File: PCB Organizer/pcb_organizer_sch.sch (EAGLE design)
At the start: 5 parts, among them J1 455-1750-1-ND, U1 ARDUINO_NANO, U2 V8FR-II, U3 POLOLU_TB67

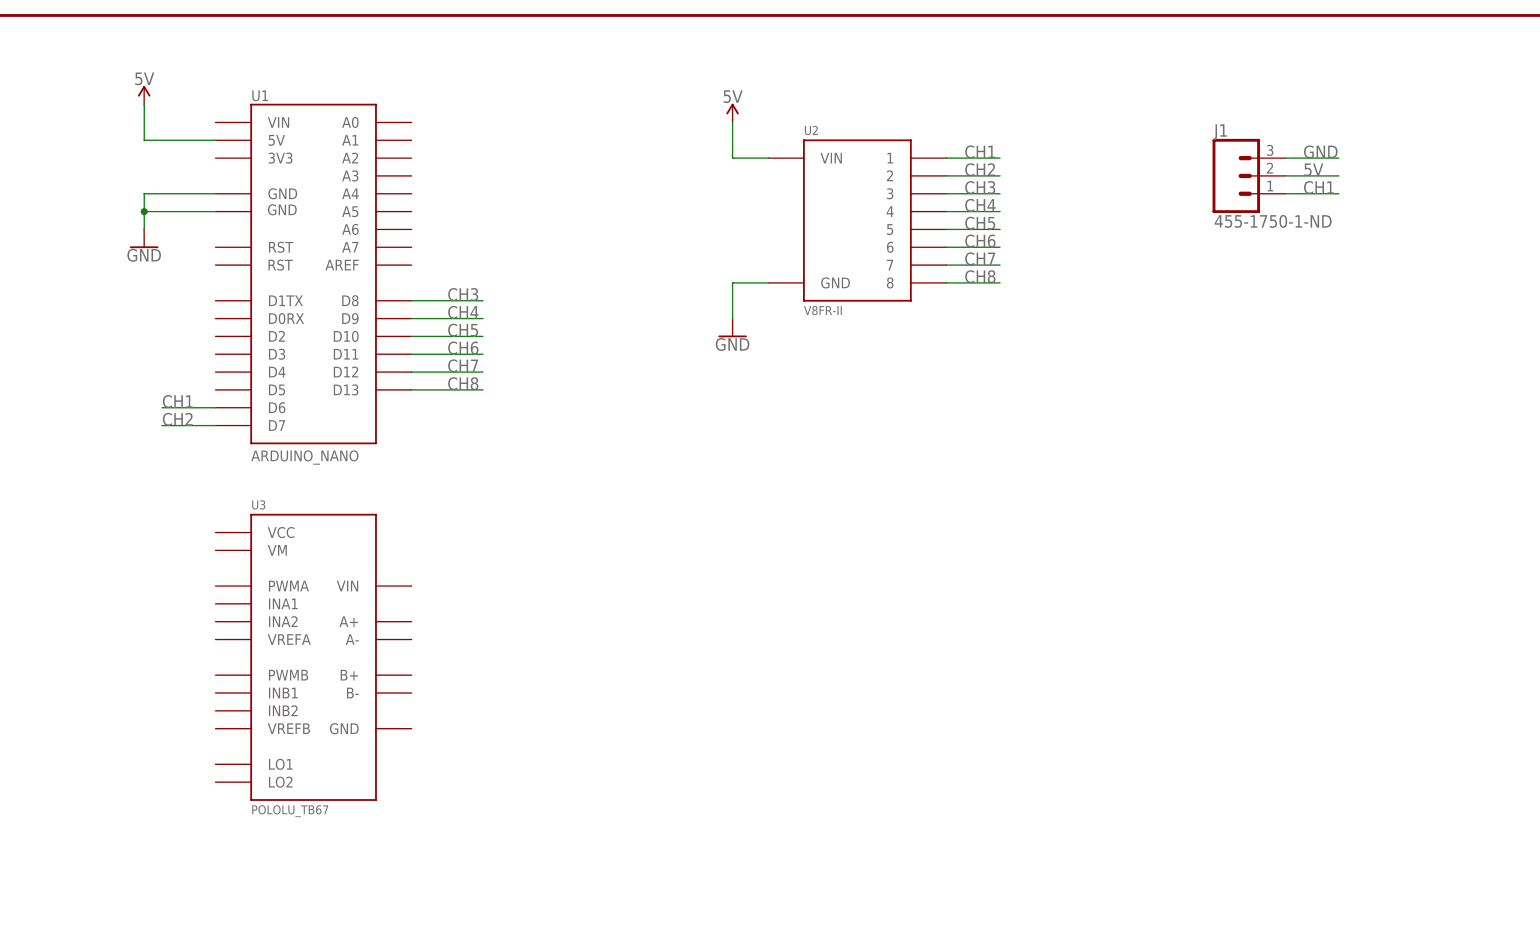
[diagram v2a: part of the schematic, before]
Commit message: Finished Schematic and laid out the board. No routing
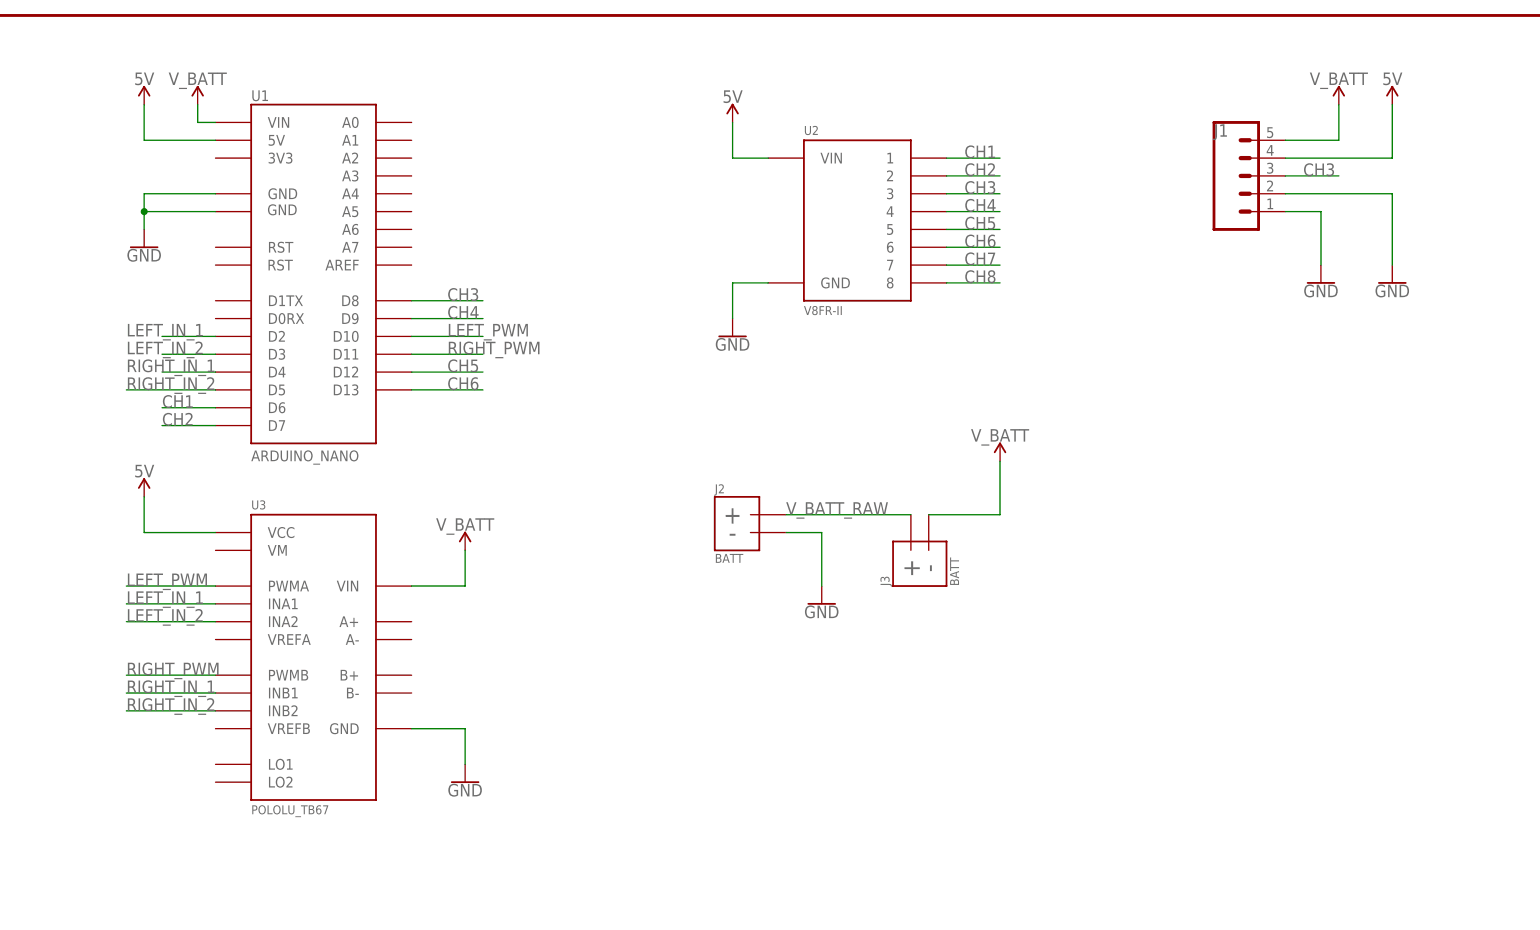
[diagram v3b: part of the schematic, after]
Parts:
- added J2, J3: BATT, CUCombatBots:BATT
- J1: device SparkFun-Connectors:CONN_03 -> SparkFun-Connectors:CONN_05
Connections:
- new net LEFT_IN_1: U1.D2, U3.INA1
- new net LEFT_IN_2: U1.D3, U3.INA2
- new net LEFT_PWM: U1.D10, U3.PWMA
- new net RIGHT_IN_1: U1.D4, U3.INB1
- new net RIGHT_IN_2: U1.D5, U3.INB2
- new net RIGHT_PWM: U1.D11, U3.PWMB
- new net V_BATT: J1.5, J3.-, U1.VIN, U3.VIN
- new net V_BATT_RAW: J2.+, J3.+
- net 5V: now also J1.4, U3.VCC; no longer J1.2
- net CH1: no longer J1.1
- net CH3: now also J1.3
- net CH5: now also U1.D12; no longer U1.D10
- net CH6: now also U1.D13; no longer U1.D11
- net CH7: no longer U1.D12
- net CH8: no longer U1.D13
- net GND: now also J1.1, J1.2, J2.-, U3.GND; no longer J1.3

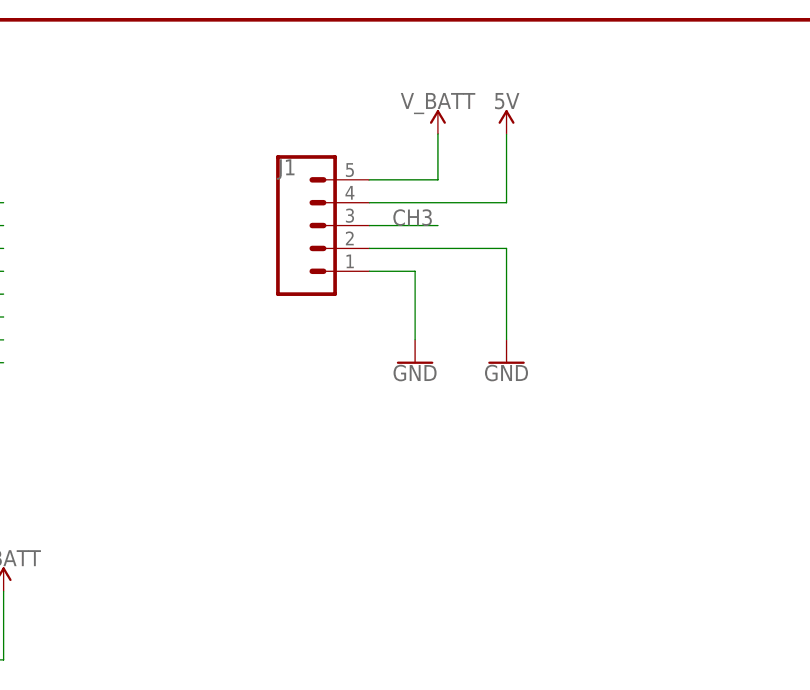
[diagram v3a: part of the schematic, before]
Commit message: Increased polygon connection trace thickness
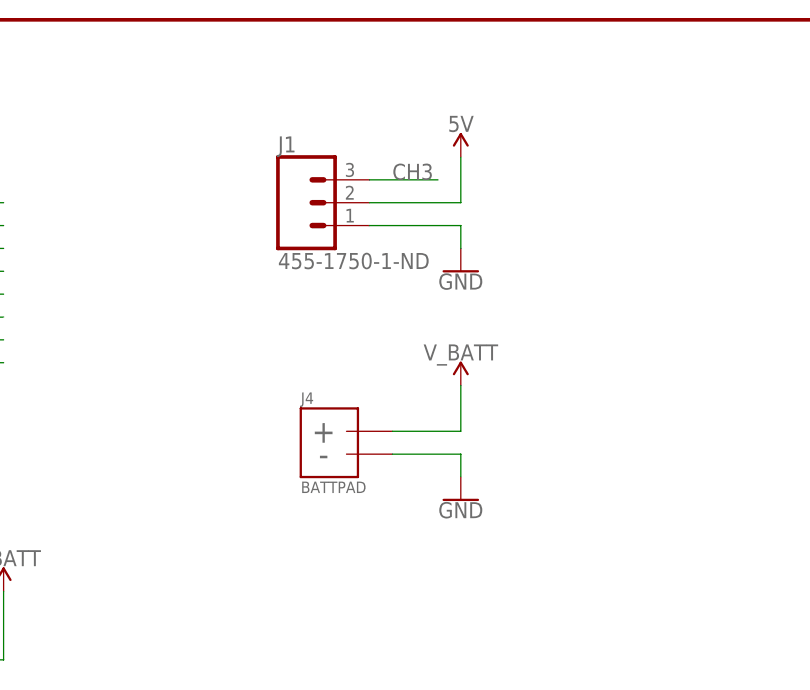
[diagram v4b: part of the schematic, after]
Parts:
- added J4: BATTPAD, CUCombatBots:BATTPAD
- J1: device SparkFun-Connectors:CONN_05 -> SparkFun-Connectors:CONN_03
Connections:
- net 5V: now also J1.2; no longer J1.4
- net GND: now also J4.-; no longer J1.2
- net V_BATT: now also J4.+; no longer J1.5

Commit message: Fixes #5, #4
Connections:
- new net V_UBEC: J1.2, U2.VIN
- net 5V: no longer J1.2, U2.VIN
- net V_BATT: no longer U1.VIN

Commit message: Fixed #1
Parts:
- J4: value BATTPAD -> BATT; device CUCombatBots:BATTPAD -> CUCombatBots:BATT
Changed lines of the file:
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@@
 <grid distance="0.1" unitdist="inch" unit="inch" style="lines" multiple="1" display="no" altdistance="0.01" altunitdist="inch" altunit="inch"/>
 <layers>
-<layer number="1" name="Top" color="4" fill="1" visible="no" active="no"/>
-<layer number="2" name="Route2" color="16" fill="1" visible="no" active="no"/>
-<layer number="3" name="Route3" color="17" fill="1" visible="no" active="no"/>
-<layer number="4" name="Route4" color="18" fill="1" visible="no" active="no"/>
-<layer number="5" name="Route5" color="19" fill="1" visible="no" active="no"/>
-<layer number="6" name="Route6" color="25" fill="1" visible="no" active="no"/>
-<layer number="7" name="Route7" color="26" fill="1" visible="no" active="no"/>
-<layer number="8" name="Route8" color="27" fill="1" visible="no" active="no"/>
-<layer number="9" name="Route9" color="28" fill="1" visible="no" active="no"/>
-<layer number="10" name="Route10" color="29" fill="1" visible="no" active="no"/>
-<layer number="11" name="Route11" color="30" fill="1" visible="no" active="no"/>
-<layer number="12" name="Route12" color="20" fill="1" visible="no" active="no"/>
-<layer number="13" name="Route13" color="21" fill="1" visible="no" active="no"/>
-<layer number="14" name="Route14" color="22" fill="1" visible="no" active="no"/>
-<layer number="15" name="Route15" color="23" fill="1" visible="no" active="no"/>
-<layer number="16" name="Bottom" color="1" fill="1" visible="no" active="no"/>
-<layer number="17" name="Pads" color="2" fill="1" visible="no" active="no"/>
-<layer number="18" name="Vias" color="2" fill="1" visible="no" active="no"/>
-<layer number="19" name="Unrouted" color="6" fill="1" visible="no" active="no"/>
-<layer number="20" name="Dimension" color="24" fill="1" visible="no" active="no"/>
-<layer number="21" name="tPlace" color="7" fill="1" visible="no" active="no"/>
-<layer number="22" name="bPlace" color="7" fill="1" visible="no" active="no"/>
-<layer number="23" name="tOrigins" color="15" fill="1" visible="no" active="no"/>
-<layer number="24" name="bOrigins" color="15" fill="1" visible="no" active="no"/>
-<layer number="25" name="tNames" color="7" fill="1" visible="no" active="no"/>
-<layer number="26" name="bNames" color="7" fill="1" visible="no" active="no"/>
-<layer number="27" name="tValues" color="7" fill="1" visible="no" active="no"/>
-<layer number="28" name="bValues" color="7" fill="1" visible="no" active="no"/>
+<layer number="1" name="Top" color="4" fill="1" visible="yes" active="no"/>
+<layer number="2" name="Route2" color="16" fill="1" visible="yes" active="no"/>
+<layer number="3" name="Route3" color="17" fill="1" visible="yes" active="no"/>
+<layer number="4" name="Route4" color="18" fill="1" visible="yes" active="no"/>
+<layer number="5" name="Route5" color="19" fill="1" visible="yes" active="no"/>
+<layer number="6" name="Route6" color="25" fill="1" visible="yes" active="no"/>
+<layer number="7" name="Route7" color="26" fill="1" visible="yes" active="no"/>
+<layer number="8" name="Route8" color="27" fill="1" visible="yes" active="no"/>
+<layer number="9" name="Route9" color="28" fill="1" visible="yes" active="no"/>
+<layer number="10" name="Route10" color="29" fill="1" visible="yes" active="no"/>
+<layer number="11" name="Route11" color="30" fill="1" visible="yes" active="no"/>
+<layer number="12" name="Route12" color="20" fill="1" visible="yes" active="no"/>
+<layer number="13" name="Route13" color="21" fill="1" visible="yes" active="no"/>
+<layer number="14" name="Route14" color="22" fill="1" visible="yes" active="no"/>
+<layer number="15" name="Route15" color="23" fill="1" visible="yes" active="no"/>
+<layer number="16" name="Bottom" color="1" fill="1" visible="yes" active="no"/>
+<layer number="17" name="Pads" color="2" fill="1" visible="yes" active="no"/>
+<layer number="18" name="Vias" color="2" fill="1" visible="yes" active="no"/>
+<layer number="19" name="Unrouted" color="6" fill="1" visible="yes" active="no"/>
+<layer number="20" name="Dimension" color="24" fill="1" visible="yes" active="no"/>
+<layer number="21" name="tPlace" color="7" fill="1" visible="yes" active="no"/>
+<layer number="22" name="bPlace" color="7" fill="1" visible="yes" active="no"/>
+<layer number="23" name="tOrigins" color="15" fill="1" visible="yes" active="no"/>
+<layer number="24" name="bOrigins" color="15" fill="1" visible="yes" active="no"/>
+<layer number="25" name="tNames" color="7" fill="1" visible="yes" active="no"/>
+<layer number="26" name="bNames" color="7" fill="1" visible="yes" active="no"/>
+<layer number="27" name="tValues" color="7" fill="1" visible="yes" active="no"/>
+<layer number="28" name="bValues" color="7" fill="1" visible="yes" active="no"/>
 <layer number="29" name="tStop" color="7" fill="3" visible="no" active="no"/>
 <layer number="30" name="bStop" color="7" fill="6" visible="no" active="no"/>
@@
 <layer number="35" name="tGlue" color="7" fill="4" visible="no" active="no"/>
 <layer number="36" name="bGlue" color="7" fill="5" visible="no" active="no"/>
-<layer number="37" name="tTest" color="7" fill="1" visible="no" active="no"/>
-<layer number="38" name="bTest" color="7" fill="1" visible="no" active="no"/>
+<layer number="37" name="tTest" color="7" fill="1" visible="yes" active="no"/>
+<layer number="38" name="bTest" color="7" fill="1" visible="yes" active="no"/>
 <layer number="39" name="tKeepout" color="4" fill="11" visible="no" active="no"/>
 <layer number="40" name="bKeepout" color="1" fill="11" visible="no" active="no"/>
@@
 <layer number="44" name="Drills" color="7" fill="1" visible="no" active="no"/>
 <layer number="45" name="Holes" color="7" fill="1" visible="no" active="no"/>
-<layer number="46" name="Milling" color="3" fill="1" visible="no" active="no"/>
-<layer number="47" name="Measures" color="7" fill="1" visible="no" active="no"/>
-<layer number="48" name="Document" color="7" fill="1" visible="no" active="no"/>
-<layer number="49" name="Reference" color="7" fill="1" visible="no" active="no"/>
-<layer number="50" name="dxf" color="7" fill="1" visible="no" active="no"/>
-<layer number="51" name="tDocu" color="7" fill="1" visible="no" active="no"/>
-<layer number="52" name="bDocu" color="7" fill="1" visible="no" active="no"/>
-<layer number="53" name="tGND_GNDA" color="7" fill="9" visible="no" active="no"/>
-<layer number="54" name="bGND_GNDA" color="1" fill="9" visible="no" active="no"/>
-<layer number="56" name="wert" color="7" fill="1" visible="no" active="no"/>
-<layer number="57" name="tCAD" color="7" fill="1" visible="no" active="no"/>
-<layer number="59" name="tCarbon" color="7" fill="1" visible="no" active="no"/>
-<layer number="60" name="bCarbon" color="7" fill="1" visible="no" active="no"/>
+<layer number="46" name="Milling" color="3" fill="1" visible="yes" active="no"/>
+<layer number="47" name="Measures" color="7" fill="1" visible="yes" active="no"/>
+<layer number="48" name="Document" color="7" fill="1" visible="yes" active="no"/>
+<layer number="49" name="Reference" color="7" fill="1" visible="yes" active="no"/>
+<layer number="50" name="dxf" color="7" fill="1" visible="yes" active="no"/>
+<layer number="51" name="tDocu" color="7" fill="1" visible="yes" active="no"/>
+<layer number="52" name="bDocu" color="7" fill="1" visible="yes" active="no"/>
+<layer number="53" name="tGND_GNDA" color="7" fill="9" visible="yes" active="no"/>
+<layer number="54" name="bGND_GNDA" color="1" fill="9" visible="yes" active="no"/>
+<layer number="56" name="wert" color="7" fill="1" visible="yes" active="no"/>
+<layer number="57" name="tCAD" color="7" fill="1" visible="yes" active="no"/>
+<layer number="59" name="tCarbon" color="7" fill="1" visible="yes" active="no"/>
+<layer number="60" name="bCarbon" color="7" fill="1" visible="yes" active="no"/>
 <layer number="88" name="SimResults" color="9" fill="1" visible="yes" active="yes"/>
 <layer number="89" name="SimProbes" color="9" fill="1" visible="yes" active="yes"/>
@@
 <part name="SUPPLY4" library="SparkFun-PowerSymbols" deviceset="5V" device="" value="V_UBEC"/>
 <part name="J1" library="SparkFun-Connectors" deviceset="CONN_03" device="" value="455-1750-1-ND"/>
-<part name="J4" library="CUCombatBots" deviceset="BATT" device="PAD" value="BATTPAD"/>
+<part name="J4" library="CUCombatBots" deviceset="BATT" device="" value="BATT"/>
 </parts>
 <sheets>
